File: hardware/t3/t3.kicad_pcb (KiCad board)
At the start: 2 copper layers, 81.3 x 45.7 mm, 83 parts, among them P1 SMA, P2 CON, P3 UART1, P4 SWD, P5 USB_B, P6 power, P7 UART2, P8 Debug, Q1 9012, SW1 SW_PUSH, SW2 SW_PUSH, U1 CC2591, U2 CC2400, U3 STM32F405RGTx, U4 LM1117-3.3, U5 LM1117-1.8, Y1 16MHz, Y2 32.768k, Y3 16MHz, t1 TST, t2 TST, t3 TST, t4 TST, t5 TST, t6 TST

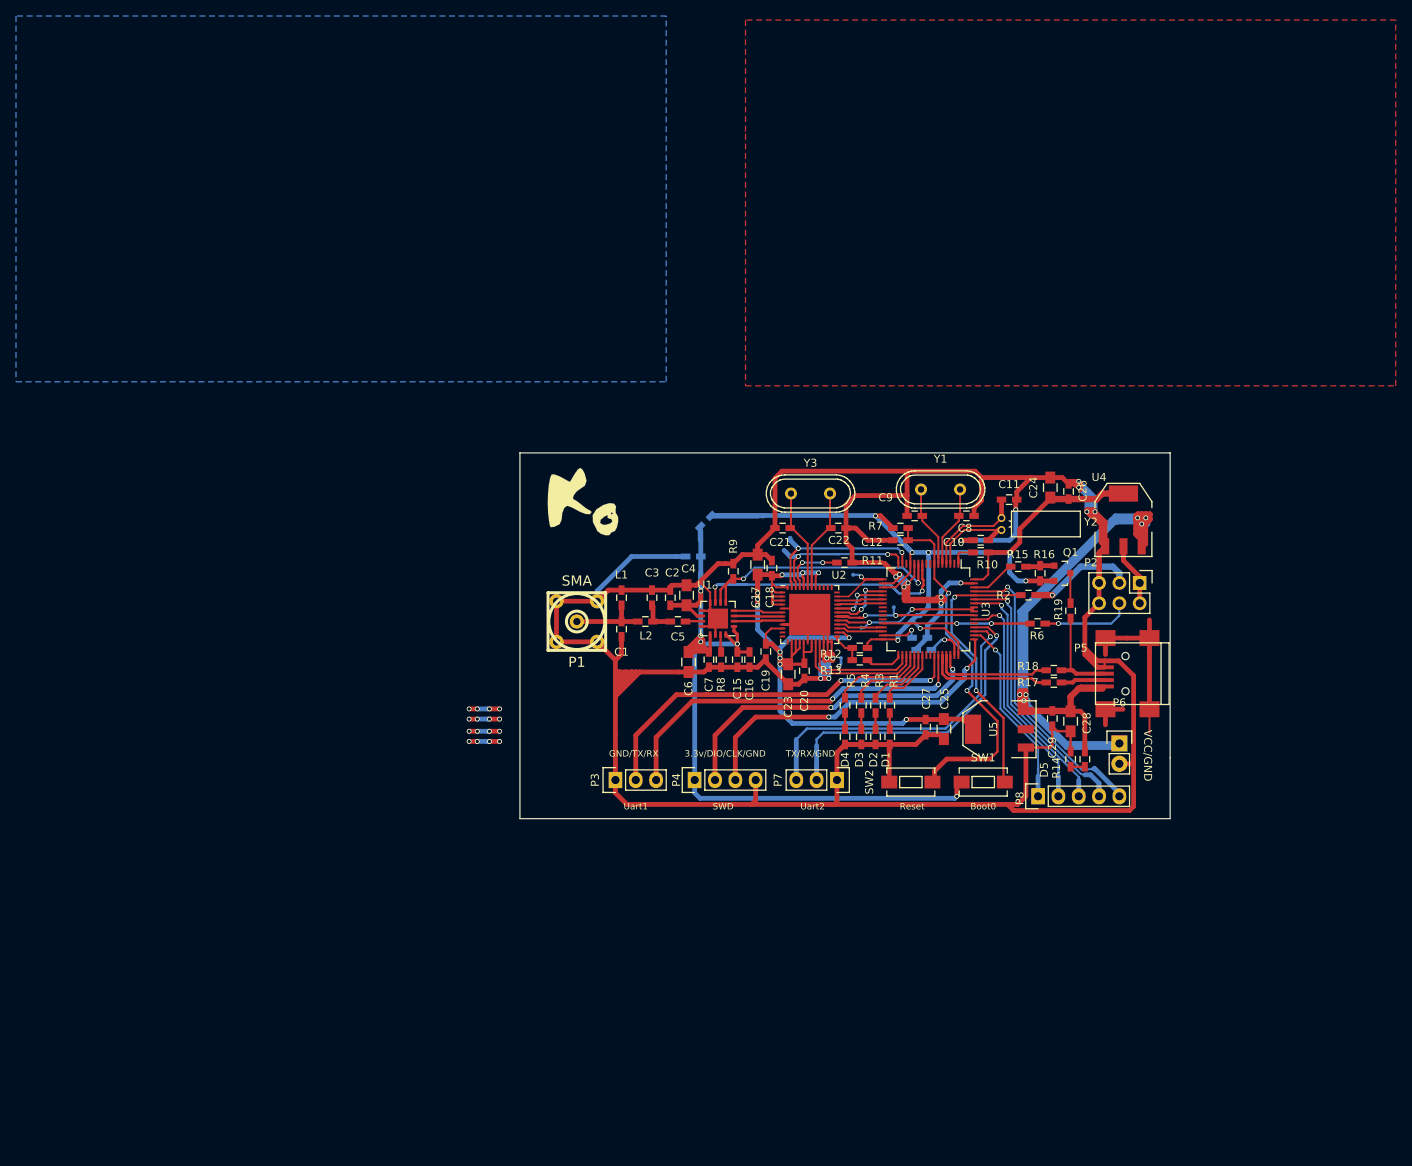
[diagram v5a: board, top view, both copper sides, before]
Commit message: firmware: update libopencm3 lib @ win7
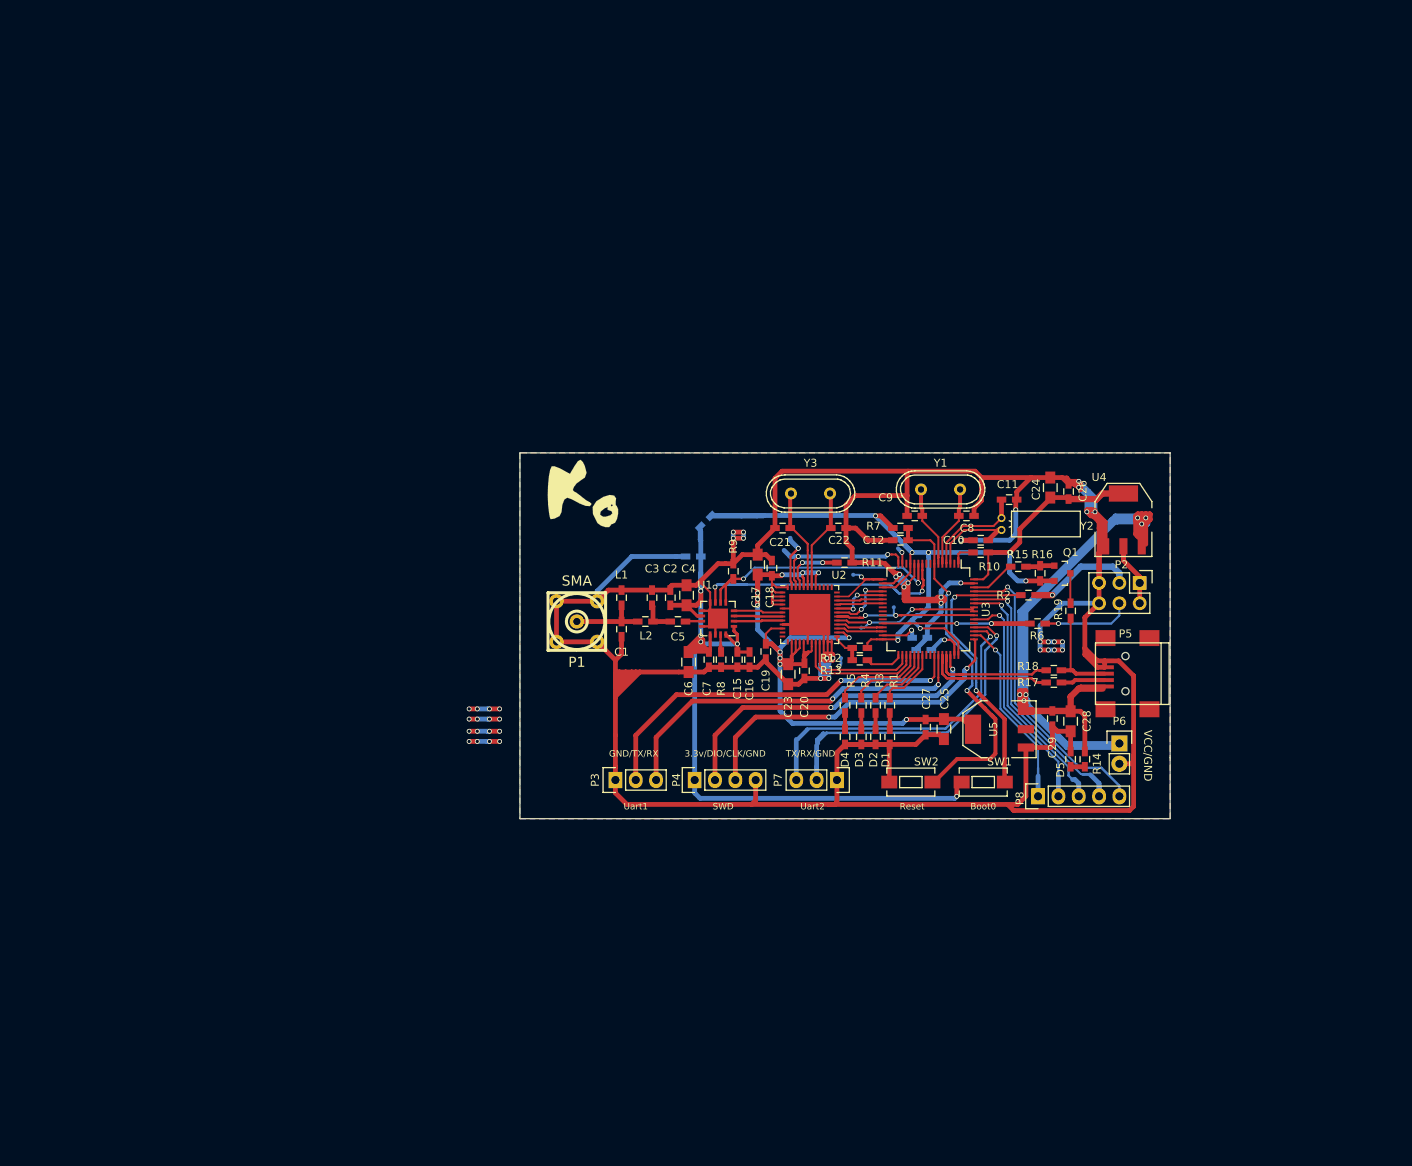
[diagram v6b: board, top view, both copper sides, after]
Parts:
- moved G*** 1.02 mm to (114.8, 81.3)
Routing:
- net GND: track 537.7 -> 579.6 mm, vias 17 -> 29
- net (no net): track 41.2 -> 15.2 mm
- net /BOOT0: track 34.3 -> 47.2 mm
- net /ATEST1: track 22.8 -> 10.3 mm
- net /BOOT1: track 17.9 -> 22.8 mm
- net Net-(C21-Pad1): track 12.8 -> 17.2 mm
- net /ATEST2: track 23.9 -> 20.4 mm
- net Net-(C9-Pad1): track 10.5 -> 12.8 mm
- net +1V8: track 109.0 -> 111.2 mm
- net /UAER2_RX: track 39.7 -> 41.8 mm
- net /UAER2_TX: track 40.7 -> 42.7 mm
- net /debug3: track 37.5 -> 38.3 mm
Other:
- board text added: "GND!!!"
